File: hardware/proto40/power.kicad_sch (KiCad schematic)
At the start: 26 parts, among them J101 USB_C_Receptacle_USB2.0_16P, Q101 BCP53, U101 USBLC6-2SC6, U102 LM66100DCK, U103 TL431DBZ, U104 AP2112K-3.3

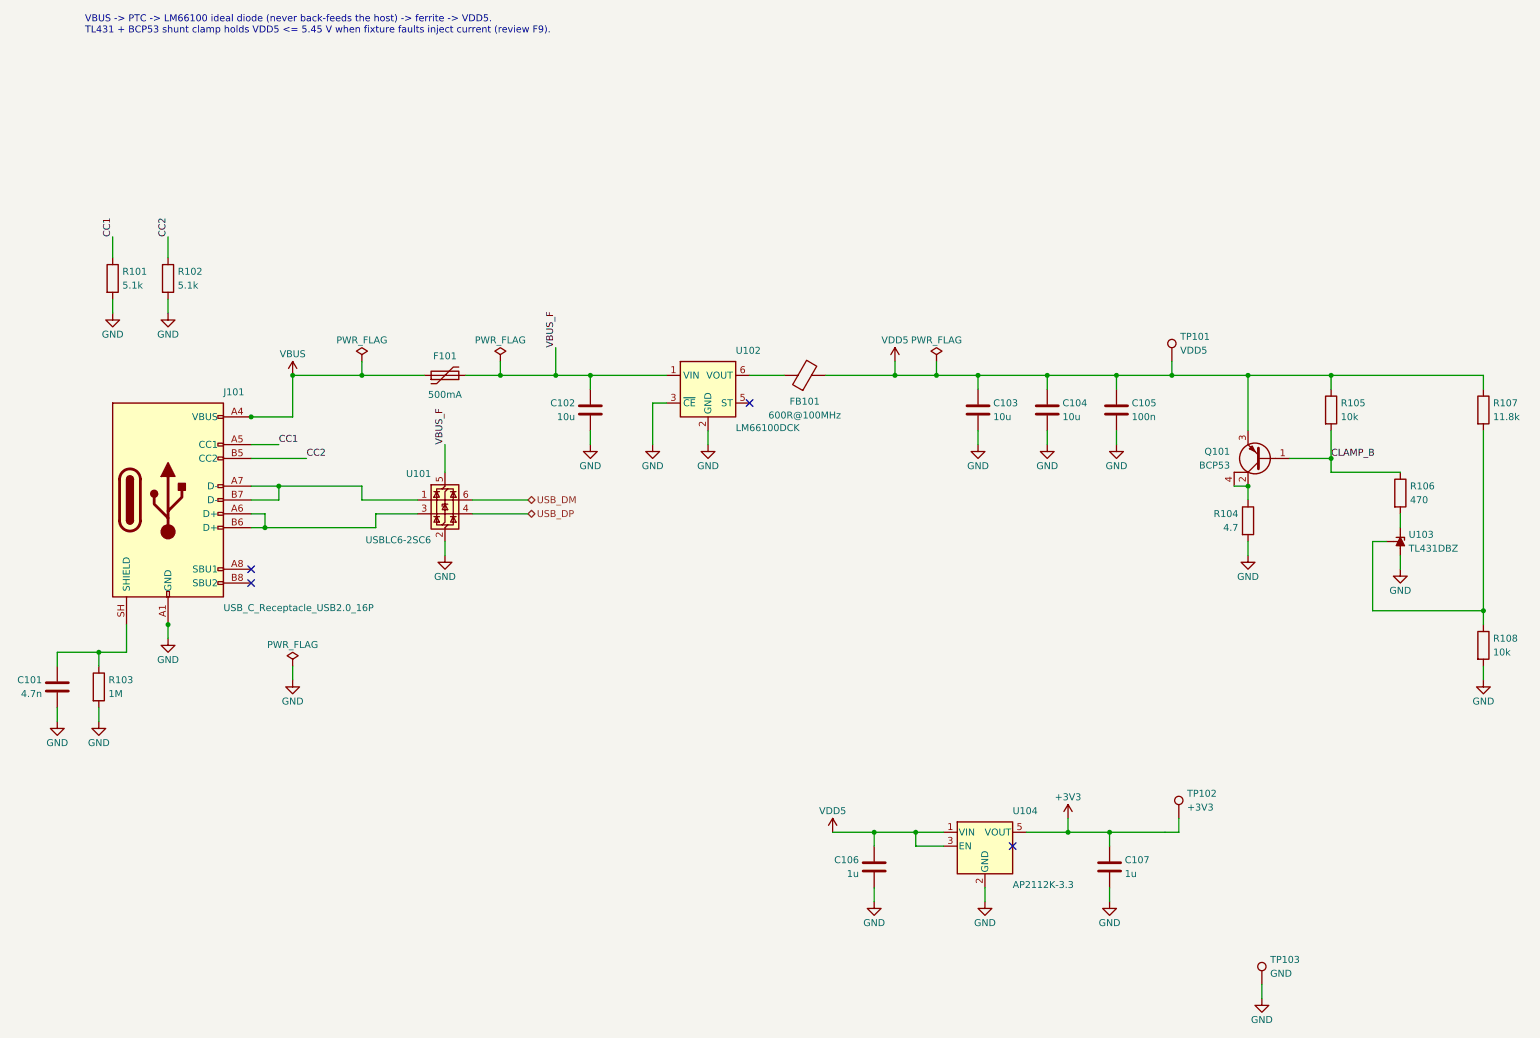
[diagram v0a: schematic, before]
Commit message: Resolve Proto40 house-style review findings
- Fixture ID lines: TVS at the connector plus series R on SDA/SCL/WP/A0/PRESENT_N;
  ID_VCC limited by 100 ohm 1206 (D14). PRESENT_N pull-up moved to MCU side.
- Shunt clamp ballast R104 is 6.8 ohm 2512, BCP53 copper note (D15).
- MPN/Manufacturer on every part (generic Yageo/Samsung passives), LCSC TBD.
- Test points on the '595 outputs and chain in/out; pull-downs on SCK/RCLK.
- Root sheet: CTRL/SENSE chains and ID lines drawn as wires; ASCII-only text.
- layoutcheck: non-ASCII, title length, text/text gap, text/wire clearance,
  NC flag on wired pin; wider char estimate. CI ERC runs --severity-all.
- Netclass patterns tightened for STIM/MUX and SPI nets.

Co-Authored-By: Claude Opus 5.5 (1M context) <noreply@anthropic.com>
Claude-Session: https://claude.ai/code/session_013SDanWEFU4wFXEYfZ6C9GH
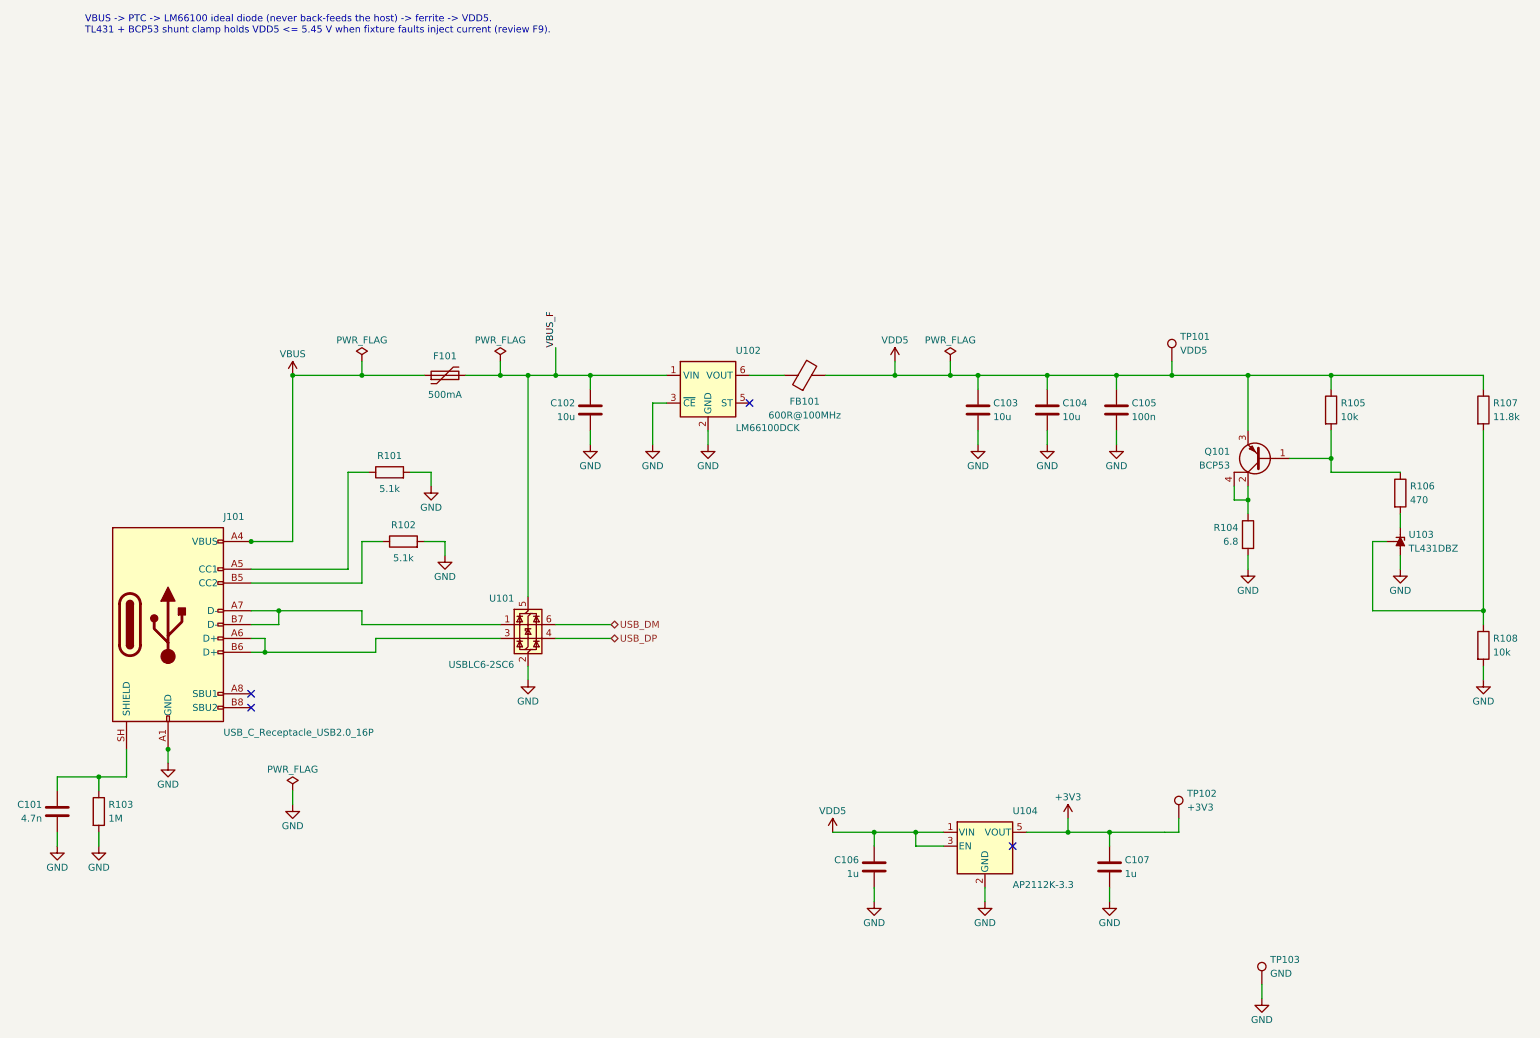
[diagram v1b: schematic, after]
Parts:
- C101: LCSC (none) -> TBD; MPN (none) -> CL10B472KC8NNNC; Manufacturer (none) -> Samsung Electro-Mechanics; Note ≥ 100 V -> >= 100 V
- C102, C103, C104: LCSC (none) -> TBD; MPN (none) -> CL21A106KAYNNNE; Manufacturer (none) -> Samsung Electro-Mechanics
- C105: LCSC (none) -> TBD; MPN (none) -> CL10B104KB8NNNC; Manufacturer (none) -> Samsung Electro-Mechanics
- C106, C107: LCSC (none) -> TBD; MPN (none) -> CL10A105KB8NNNC; Manufacturer (none) -> Samsung Electro-Mechanics
- F101: LCSC (none) -> TBD; MPN 1206 PTC 500 mA hold, 6 V -> 1206L050YR; Manufacturer (none) -> Littelfuse; Note (none) -> 500 mA hold, 6 V
- FB101: LCSC (none) -> TBD; MPN (none) -> BLM18KG601SN1D; Manufacturer (none) -> Murata; Note ≥ 1 A -> >= 1 A
- J101: LCSC (none) -> TBD; MPN (none) -> HC-TYPE-C-16P-01A; Manufacturer (none) -> HCTL
- Q101: LCSC (none) -> TBD; Manufacturer (none) -> Nexperia; Note shunt pass, ≥ 1 W -> shunt pass, up to ~1 W at 300 mA: >= 1 cm2 collector copper
- R101, R102: LCSC (none) -> TBD; MPN (none) -> RC0603FR-075K1L; Manufacturer (none) -> Yageo; Note (none) -> USB-C Rd
- R103: LCSC (none) -> TBD; MPN (none) -> RC0603FR-071ML; Manufacturer (none) -> Yageo
- R104: value 4.7 -> 6.8; footprint Resistor_SMD:R_1206_3216Metric -> Resistor_SMD:R_2512_6332Metric; LCSC (none) -> TBD; MPN (none) -> RC2512FK-076R8L; Manufacturer (none) -> Yageo; Note collector ballast -> collector ballast, 0.6 W at 300 mA (1 W part)
- R105, R108: LCSC (none) -> TBD; MPN (none) -> RC0603FR-0710KL; Manufacturer (none) -> Yageo
- R106: LCSC (none) -> TBD; MPN (none) -> RC0603FR-07470RL; Manufacturer (none) -> Yageo
- R107: LCSC (none) -> TBD; MPN (none) -> RC0603FR-0711K8L; Manufacturer (none) -> Yageo
- TP101, TP102, TP103: LCSC (none) -> none; MPN (none) -> none (PCB pad only)
- U101: LCSC (none) -> TBD; Manufacturer (none) -> STMicroelectronics
- U102, U103: LCSC (none) -> TBD; Manufacturer (none) -> Texas Instruments
- U104: LCSC (none) -> TBD; Manufacturer (none) -> Diodes Incorporated
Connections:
- net CC1: no longer names the net of J101.A5 (CC1), R101.1
- net CC2: no longer names the net of J101.B5 (CC2), R102.1
- net CLAMP_B: no longer names the net of Q101.1 (B), R105.2, R106.1
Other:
- title: Proto40 – USB-C power, VDD5 shunt clamp, 3.3 V -> Proto40 - USB-C power, VDD5 shunt clamp, 3.3 V
- moved on the sheet: C101, J101, R101, R102, R103, R104, U101
